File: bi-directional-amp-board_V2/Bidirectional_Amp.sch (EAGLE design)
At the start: 102 parts, among them J1 142-0701-851_ALT, J2 142-0701-851_ALT, J3 142-0701-851_ALT, J4 142-0701-851_ALT, J6 142-0701-851_ALT, J7 142-0701-851_ALT, U1 SN74LVC1G32DBVR, U10 TQP9111, U11 SN74LV1T34DBVR, U2 LTC6994-1, U3 LTC6994-1, U4 TQP3M903X, U5 TQP3M903X, U7 QPC1022, U8 QPC1022, U9 SN74LV1T34DBVR

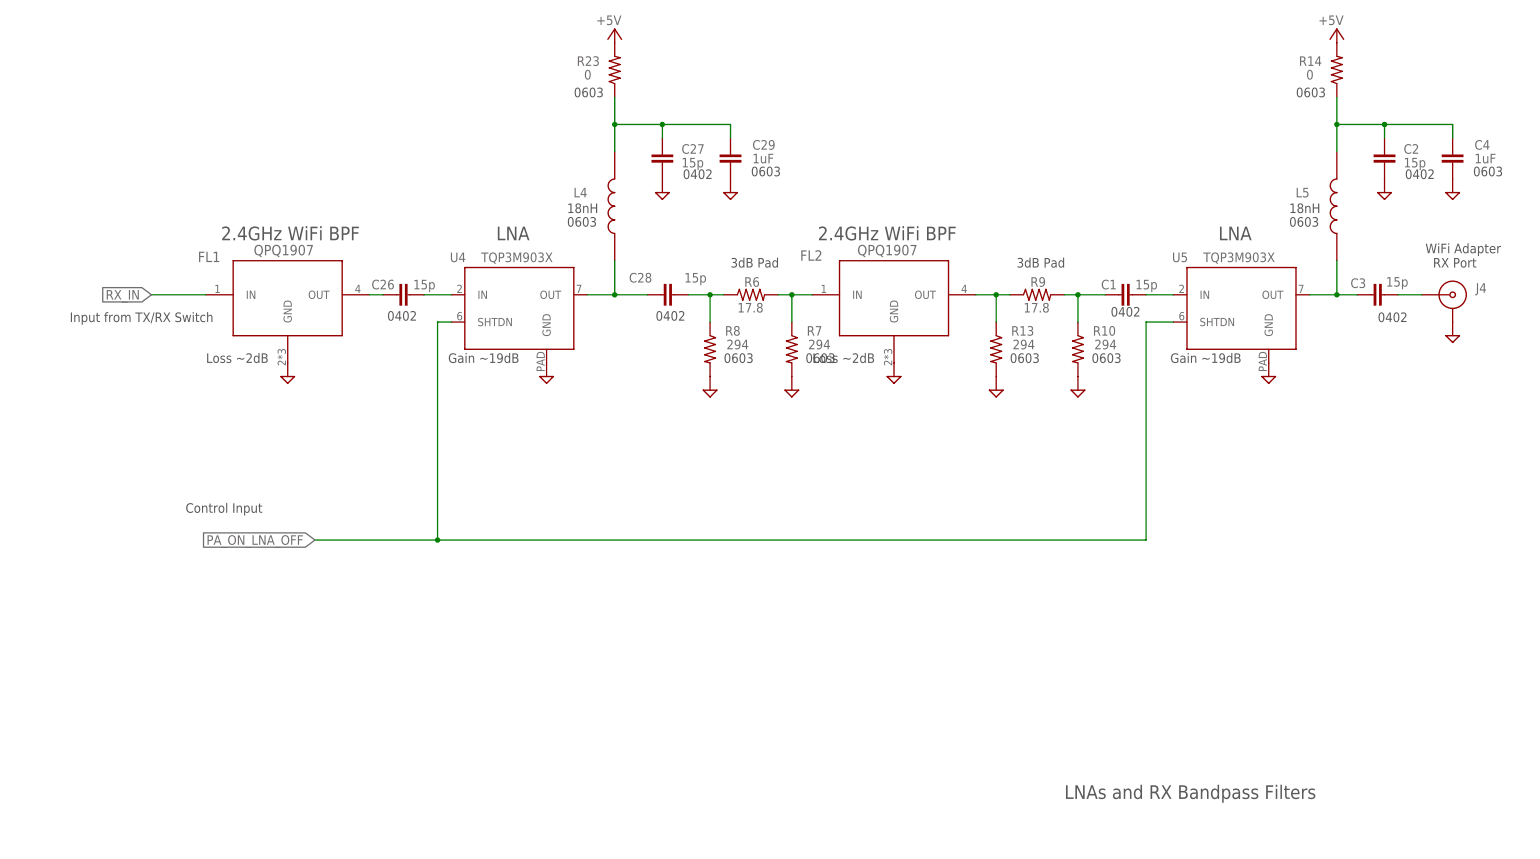
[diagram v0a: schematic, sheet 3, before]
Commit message: V2 version of board after design review, also adds block diagram
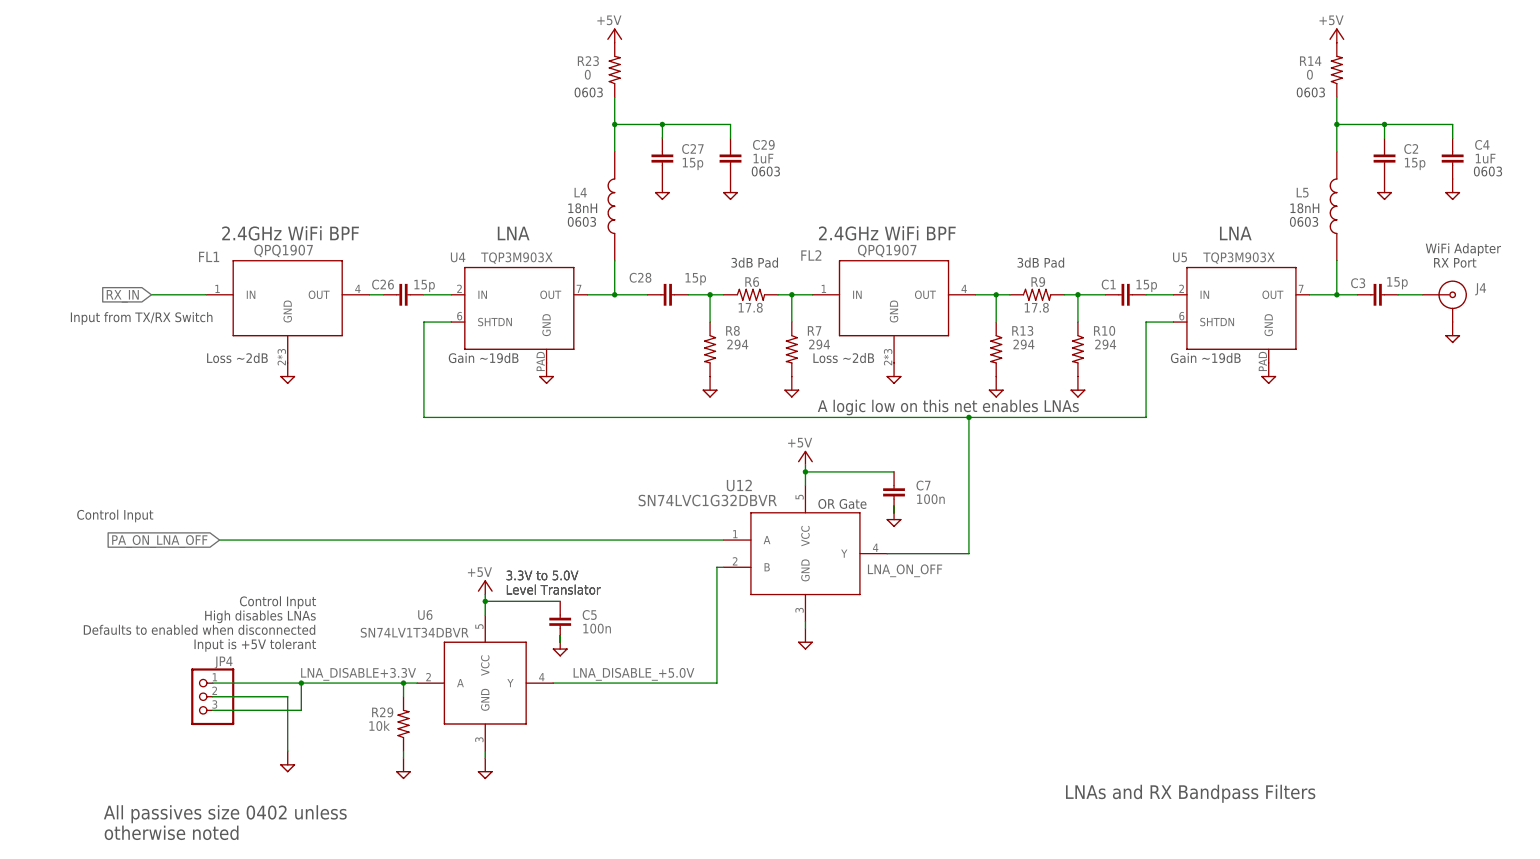
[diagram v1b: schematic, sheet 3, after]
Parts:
- removed C13, C36, C40: 100p, oresat-rcl:C-EU0402-B-NOSILK
- added JP4: (no value), pinhead:PINHD-1X3
- added R29: 10k, oresat-rcl:R-US_0402-B-NOSILK
- added U12: SN74LVC1G32DBVR, SN74LVC1G32DBVR:SN74LVC1G32DBVR
- added U6: SN74LV1T34DBVR, SamacSys_Parts:SN74LV1T34DBVR
- C15, C16, C17: device rcl:C-EUC0603 -> oresat-rcl:C-EU0402-B-NOSILK; MFR Kemet -> TDK; MPN C0603C104K5RACAUTO -> CGA2B1X7R1C104K050BC
- C18: device rcl:C-EUC0603 -> oresat-rcl:C-EU0402-B-NOSILK; MPN GCM1885C1H101JA16D -> GCM1555C1H101JA16D
- C19: device rcl:C-EUC0603 -> oresat-rcl:C-EU0402-B-NOSILK; MPN CGA3E2C0G1H102J080AA -> CGA2B2NP01H102J050BA
- C32: MPN GCM1555C1H101JA16D -> (none)
- C5: value 100p -> 100n; MFR Murata -> TDK Corporation; MPN GCM1555C1H101JA16D -> CGA2B1X7R1C104K050BC
- C7: value 100p -> 100n; MFR Murata -> TDK; MPN GCM1555C1H101JA16D -> CGA2B1X7R1C104K050BC
- R10, R13, R7, R8: device rcl:R-US_R0603 -> oresat-rcl:R-US_0402-B-NOSILK; MPN ERJ-3EKF2940V -> ERJ-2RKF2940X
- R19: device rcl:R-US_R0603 -> oresat-rcl:R-US_0402-B-NOSILK; MPN ERJ-3EKF1100V -> ERJ-2RKF1100X
- R32, R36: value 620 -> 1k; MPN ERJ-2GEJ621X -> ERJ-2GEJ102X
- R6, R9: device rcl:R-US_R0603 -> oresat-rcl:R-US_0402-B-NOSILK; MPN ERJ-3EKF17R8V -> ERJ-2RKF17R8X
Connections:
- new net LNA_DISABLE+3.3V: JP4.1, JP4.3, R29.2, U6.A
- new net LNA_DISABLE_+5.0V: U12.B, U6.Y
- new net LNA_ON_OFF: U12.Y, U4.SHTDN, U5.SHTDN
- net +5V: now also U12.VCC, U6.VCC; no longer C13.1, C36.1, C40.1
- net GND: now also JP4.2, R29.1, U12.GND, U6.GND; no longer C13.2, C36.2, C40.2
- net PA_ON_LNA_OFF: now also U12.A; no longer U4.SHTDN, U5.SHTDN
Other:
- note added: "A logic low on this net enables LNAs"
- note added: "All passives size 0402 unless otherwise noted"
- note added: "Control Input High disables LNAs Defaults to enabled when disconnected Input is +5V tolerant"
- note added: "Do not hot switch!"
- note removed: "0402"
- moved on the sheet: C14, C39, C41, C6, C8

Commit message: Prepping for Rev.2 layout.
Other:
- moved on the sheet: C10, C12, C30, C31, C32, C33, C9, J3, R15, R16, R24, R25

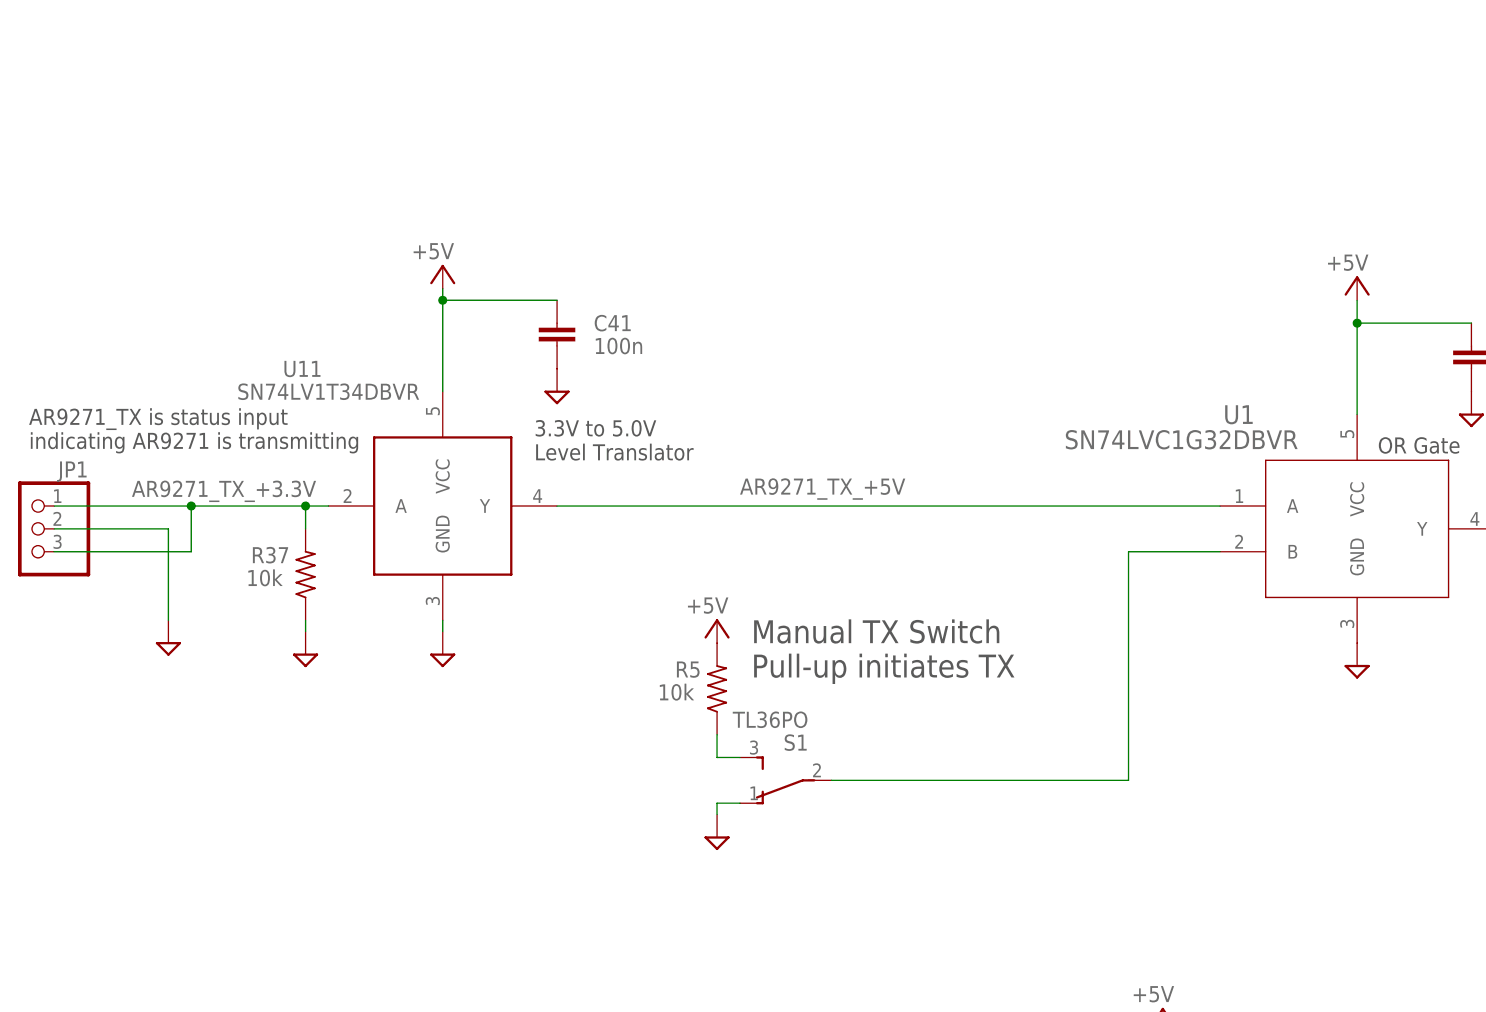
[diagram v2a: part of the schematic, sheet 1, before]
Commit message: Check in for Vigely to do some modeling. All routed, but not yet polished.
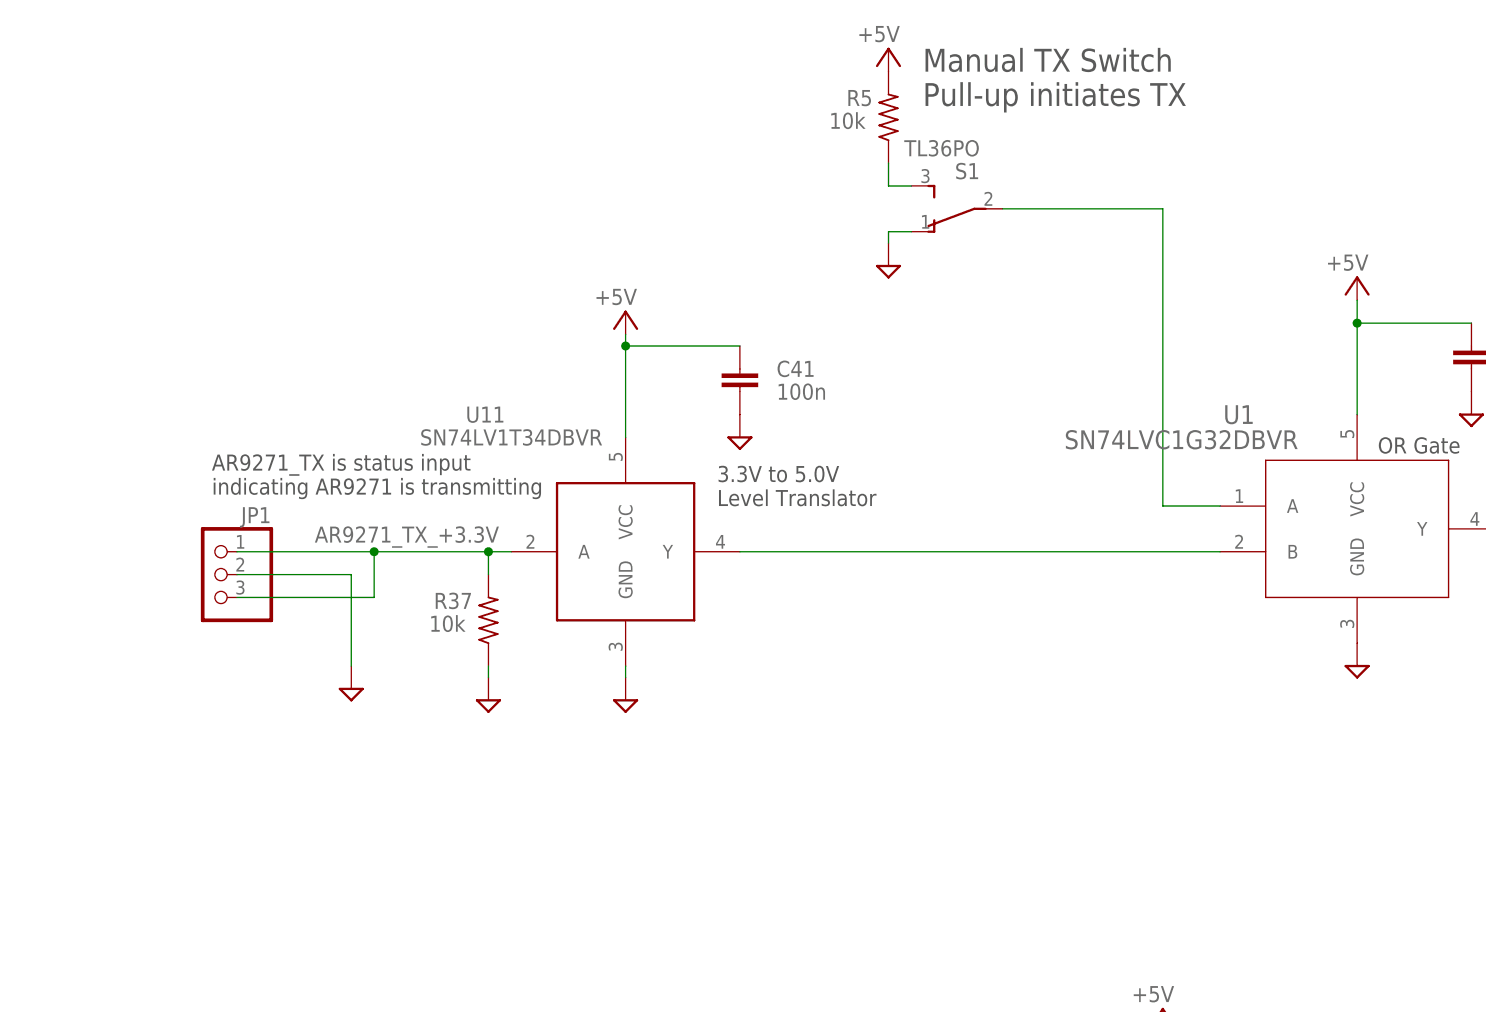
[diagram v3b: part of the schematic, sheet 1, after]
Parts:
- removed JP2: (no value), pinhead:PINHD-1X8
- added JP6: (no value), pinhead:PINHD-1X4
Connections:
- net N$13 renamed AS-EN
- net N$17 renamed AS-CTRL
- net N$18 renamed HELICAL
- net N$23 renamed TURNSTILE
- net N$32 renamed TXRX-EN
- net N$34 renamed TXRX-CTRL
- net N$47 renamed THROUGH
- removed net AR9271_TX_+5V: U1.A, U11.Y
- removed net N$36: C35.1, JP2.3, JP2.4
- removed net N$43: C34.1, JP2.7
- new net N$13: U1.B, U11.Y
- net +5V: now also C34.1, C35.1, JP6.1, JP6.2; no longer JP2.5
- net GND: now also JP6.3, JP6.4; no longer JP2.1, JP2.2
- net N$5: now also U1.A; no longer U1.B
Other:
- note removed: "+5VDC lab supply"
- note removed: "+5VDC to all loads"
- note removed: "DC/DC Conv !SHDN!"
- note removed: "DC/DC Conv In"
- note removed: "DC/DC Conv Out"
- note removed: "Ground"
- note removed: "Power supply section awaiting decision on battery bus voltage"
- note removed: "To use DC/DC Converter for +5VDC, connect Vbatt source to Pin 7 and connect Ground to Pin 1 or 2. Connect Pin 6 to Pin 5 with jumper clip. To use lab supply, connect +5VDC to Pin 3 and connect Ground to Pin 1 or 2. Connect Pin 4 to Pin 5 with jumper clip. Pin 8 may be left unconnected unless an external shutdown feature is needed."
- moved on the sheet: C34, C35, C41, JP1, R37, R5, S1, U11

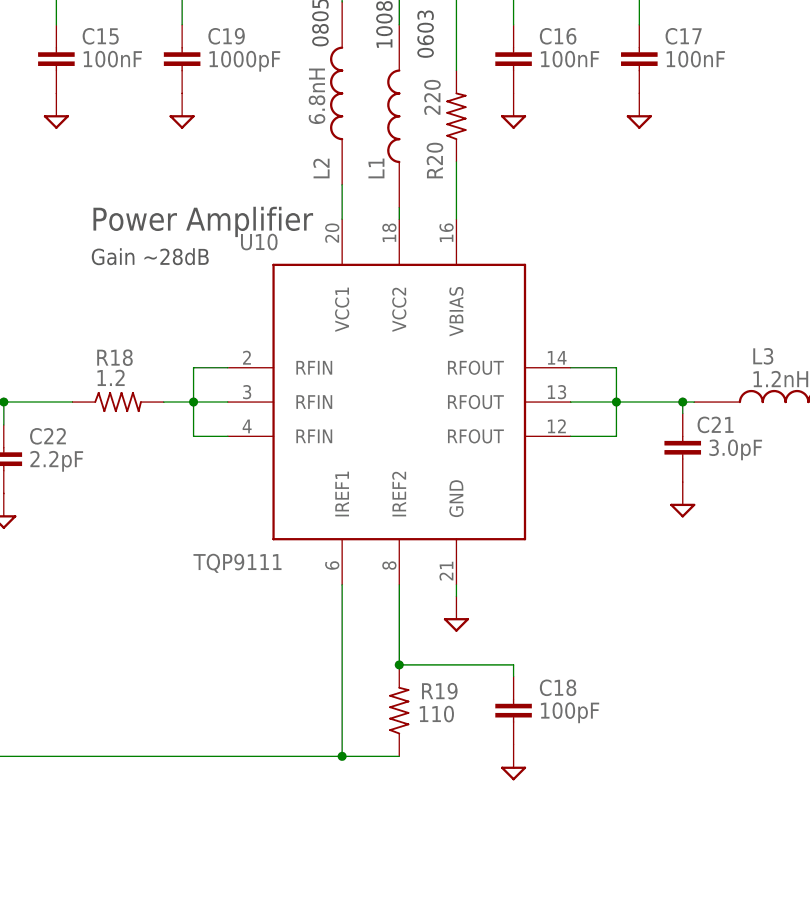
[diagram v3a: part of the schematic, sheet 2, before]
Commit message: Finished layout! More vias, fixed Vpd issue for LNAs, cleaned up tnames, etc etc.
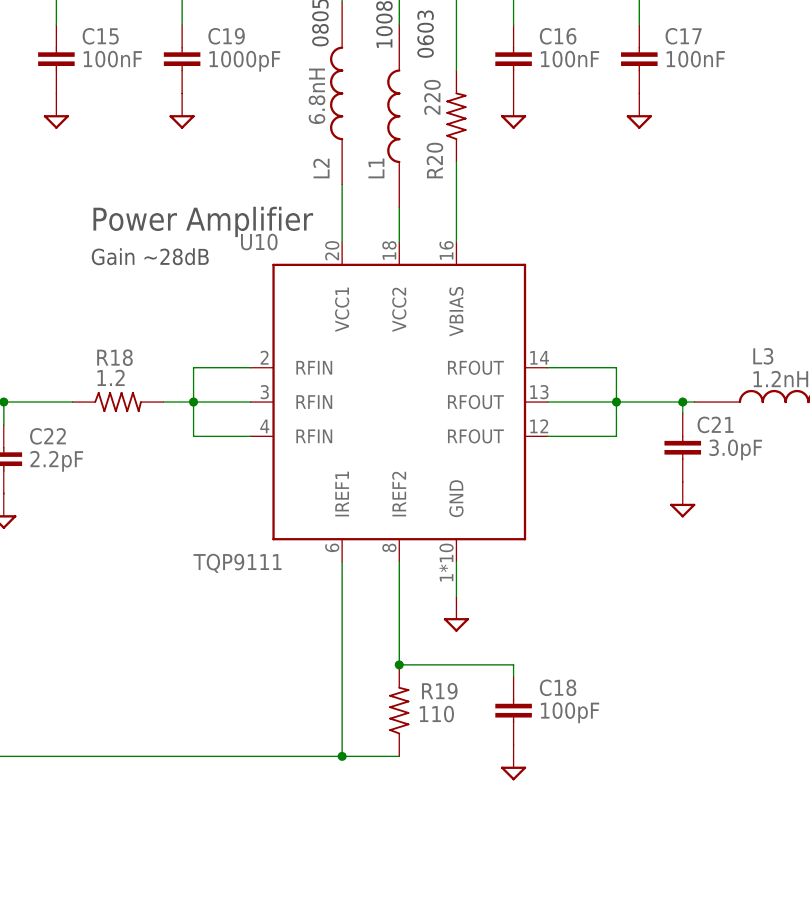
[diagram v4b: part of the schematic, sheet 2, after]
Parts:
- added R30: 33k, oresat-rcl:R-US_0402-B-NOSILK
- added R31: 10k, oresat-rcl:R-US_0402-B-NOSILK
- C1, C21, C22, C23, C26, C28, C3: device oresat-rcl:C-EU0402-B-NOSILK -> oresat-rcl:C-EU0402-C-NOSILK
- C20, C24: device rcl:C-EUC0603 -> oresat-rcl:C-EU0603-C-NOSILK
- C29, C4: device rcl:C-EUC0603 -> oresat-rcl:C-EU0603-B-NOSILK
- R1, R2, R20, R3, R4: device rcl:R-US_R0603 -> oresat-rcl:R-US_0603-C-NOSILK
- R10, R13, R6, R7, R8, R9: device oresat-rcl:R-US_0402-B-NOSILK -> oresat-rcl:R-US_0402-C-NOSILK
- R14, R23: device rcl:R-US_R0603 -> oresat-rcl:R-US_0603-B-NOSILK
- U10: device SamacSys_Parts:TQP9111 -> oresat-samacsys_Parts:TQP9111
- renumbered S1 to SW1
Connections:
- new net N$17: R30.2, U12.Y
- net GND: now also R31.2
- net LNA_ON_OFF: now also R30.1, R31.1; no longer U12.Y
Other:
- note added: "Logic high disables (shutdowns) the LNAs"
- note removed: "A logic low on this net enables LNAs"
- moved on the sheet: U10
